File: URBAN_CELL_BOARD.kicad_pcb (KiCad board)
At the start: 2 copper layers, 162 x 171.6 mm, 15 parts, among them J1 Conn_02x09_Odd_Even, J2 Conn_01x02_Female, J3 Conn_01x02_Female

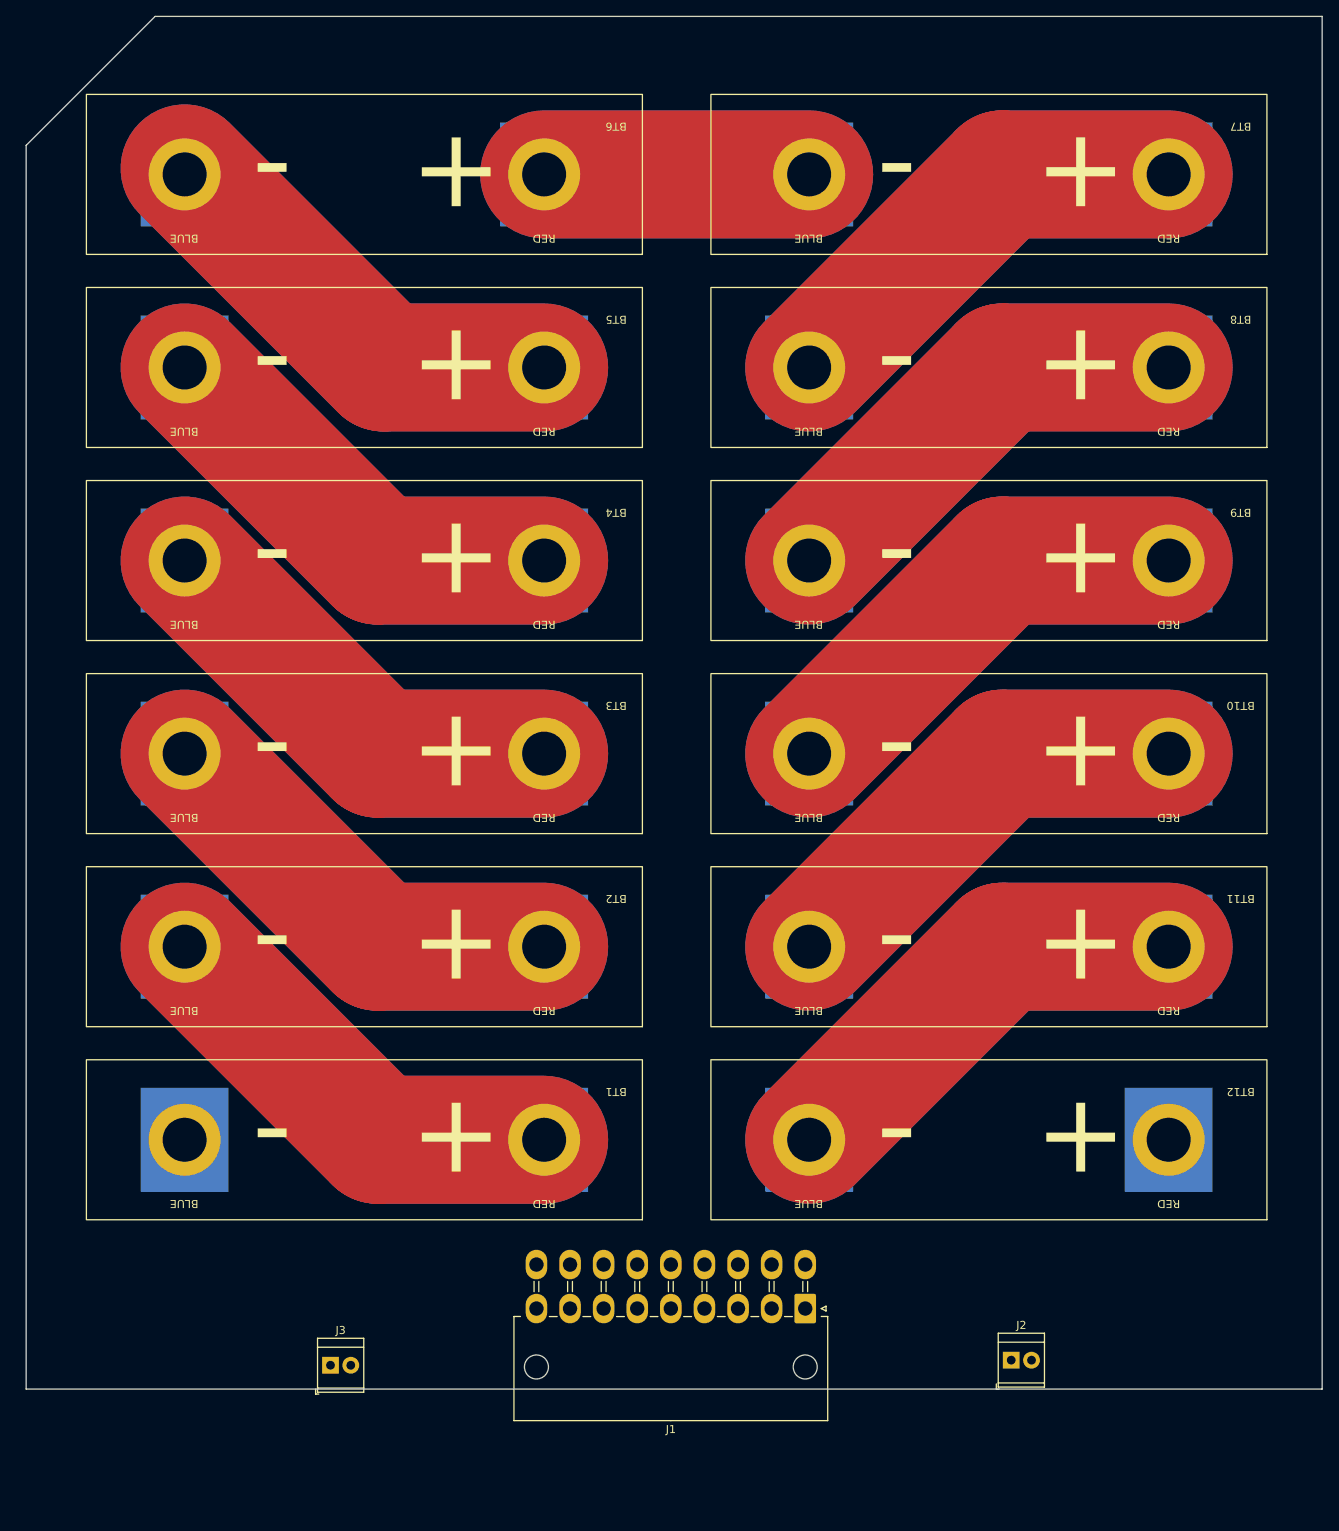
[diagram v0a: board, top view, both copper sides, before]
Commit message: fixed connector footprints, edited connector symbols, added mounting holes, solved DRC routing issue, created 48V and GND filled zones around one connector, made silkscreen edits
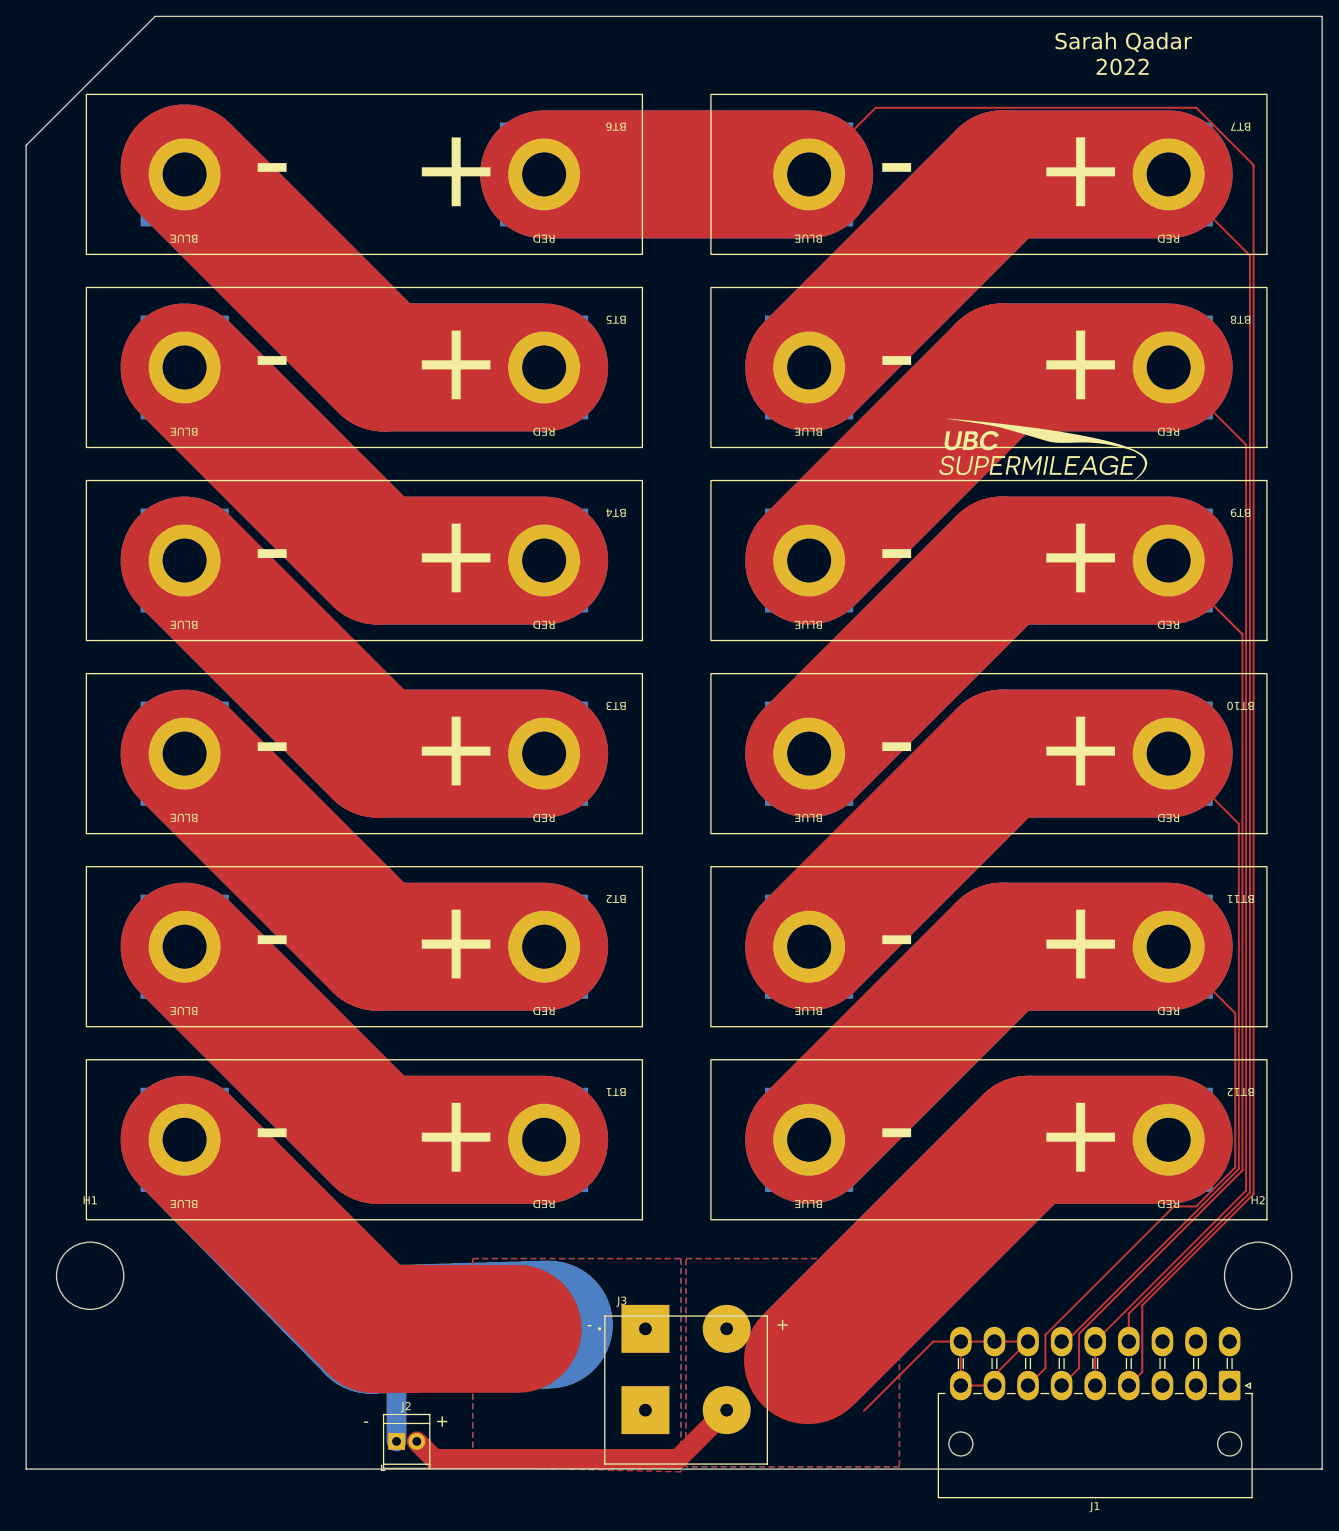
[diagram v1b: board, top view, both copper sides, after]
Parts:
- added G***: LOGO, LOGO, F.Cu at (210.8, 154.9)
- added H1: MountingHole, MountingHole:MountingHole_8.4mm_M8, F.Cu at (91.9, 257.4)
- added H2: MountingHole, MountingHole:MountingHole_8.4mm_M8, F.Cu at (237.9, 257.4)
- J3: footprint TerminalBlock_TE-Connectivity:TerminalBlock_TE_282834-2_1x02_P2.54mm_Horizontal -> TerminalBlock_TE-Connectivity:TE_1986660-2
- moved J2 77.5 mm to (130.2, 278.1)
- moved J1 53.9 mm to (234.3, 271.1)
- moved J3 39.6 mm to (161.3, 264.1)
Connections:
- J1 pad 10: cell8+ -> cell1+
- J1 pad 11: cell9+ -> cell3+
- J1 pad 12: cell10+ -> cell5+
- J1 pad 13: cell11+ -> cell7+
- J1 pad 14: +48V -> cell8+
- J1 pad 15: +48V -> cell10+
- J1 pad 2: cell1+ -> cell2+
- J1 pad 3: cell2+ -> cell4+
- J1 pad 4: cell3+ -> cell6+
- J1 pad 5: cell4+ -> cell8+
- J1 pad 6: cell5+ -> cell9+
- J1 pad 7: cell6+ -> cell11+
- J1 pad 8: cell7+ -> +48V
- J1 pad 9: cell8+ -> +48V
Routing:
- net cell6+: track 66.3 -> 287.2 mm
- net +48V: track 0.00 -> 198.6 mm
- net cell7+: track 109.9 -> 266.2 mm
- net cell8+: track 109.9 -> 249.0 mm
- net GND: track 0.00 -> 122.2 mm
- net cell9+: track 109.9 -> 226.2 mm
- net cell10+: track 109.9 -> 196.5 mm
- net cell11+: track 109.9 -> 180.5 mm
- added copper zone on B.Cu, net +48V
- added copper zone on F.Cu, net +48V
- added copper zone on B.Cu, net GND
- added copper zone on F.Cu, net GND
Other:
- board size 162 x 171.6 mm -> 162 x 181.6 mm
- board text added: "+"
- board text added: "-"
- board text added: "Sarah Qadar 2022"

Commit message: routed traces
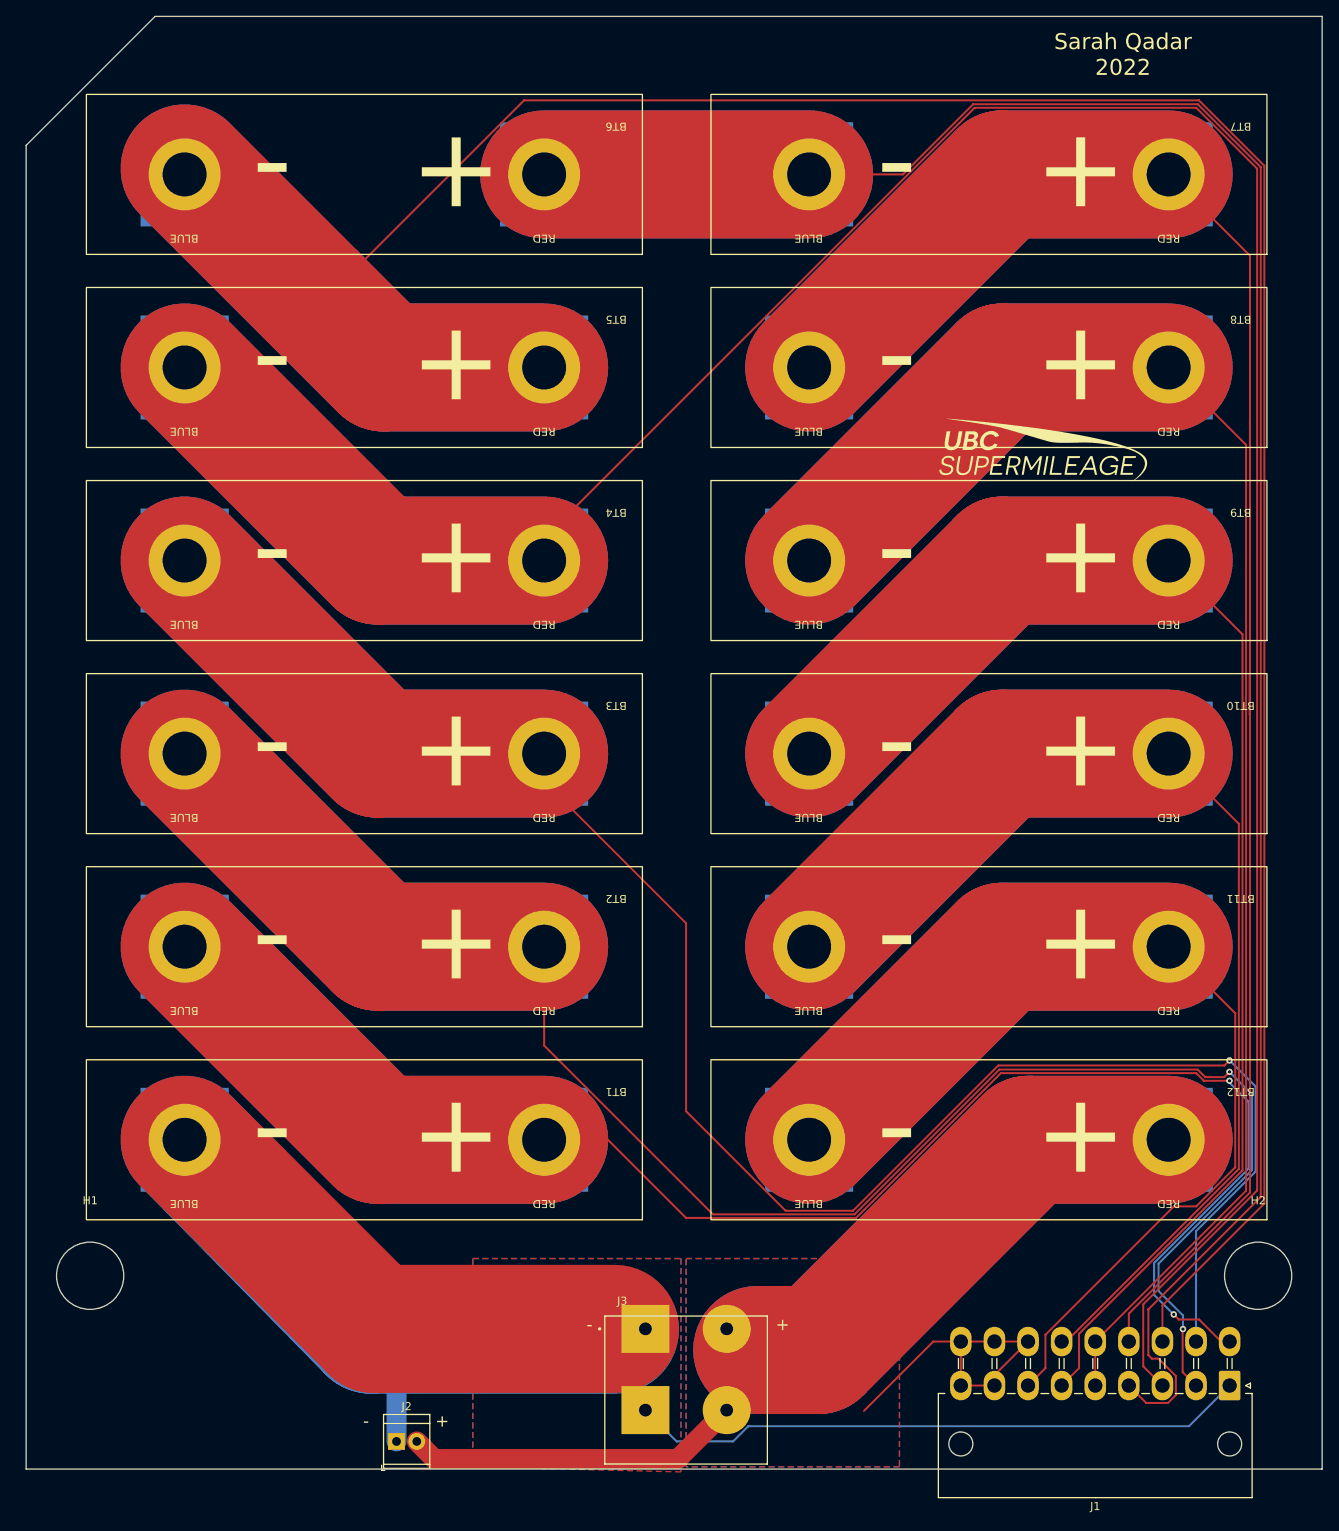
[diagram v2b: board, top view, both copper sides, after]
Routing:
- net cell5+: track 110.5 -> 395.1 mm
- net cell4+: track 109.9 -> 386.2 mm
- net cell3+: track 109.9 -> 282.4 mm, vias 0 -> 1
- net cell2+: track 109.9 -> 272.0 mm, vias 0 -> 2
- net cell1+: track 109.9 -> 252.0 mm, vias 0 -> 2
- net GND: track 122.2 -> 220.2 mm
- net cell7+: track 266.2 -> 303.1 mm
- net cell6+: track 287.2 -> 298.0 mm
- net +48V: track 198.6 -> 209.4 mm
